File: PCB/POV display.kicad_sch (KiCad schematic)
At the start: 23 parts, among them U1 ESP32-C3FH4, U2 SC7A20, X1 40MHz, 15pF

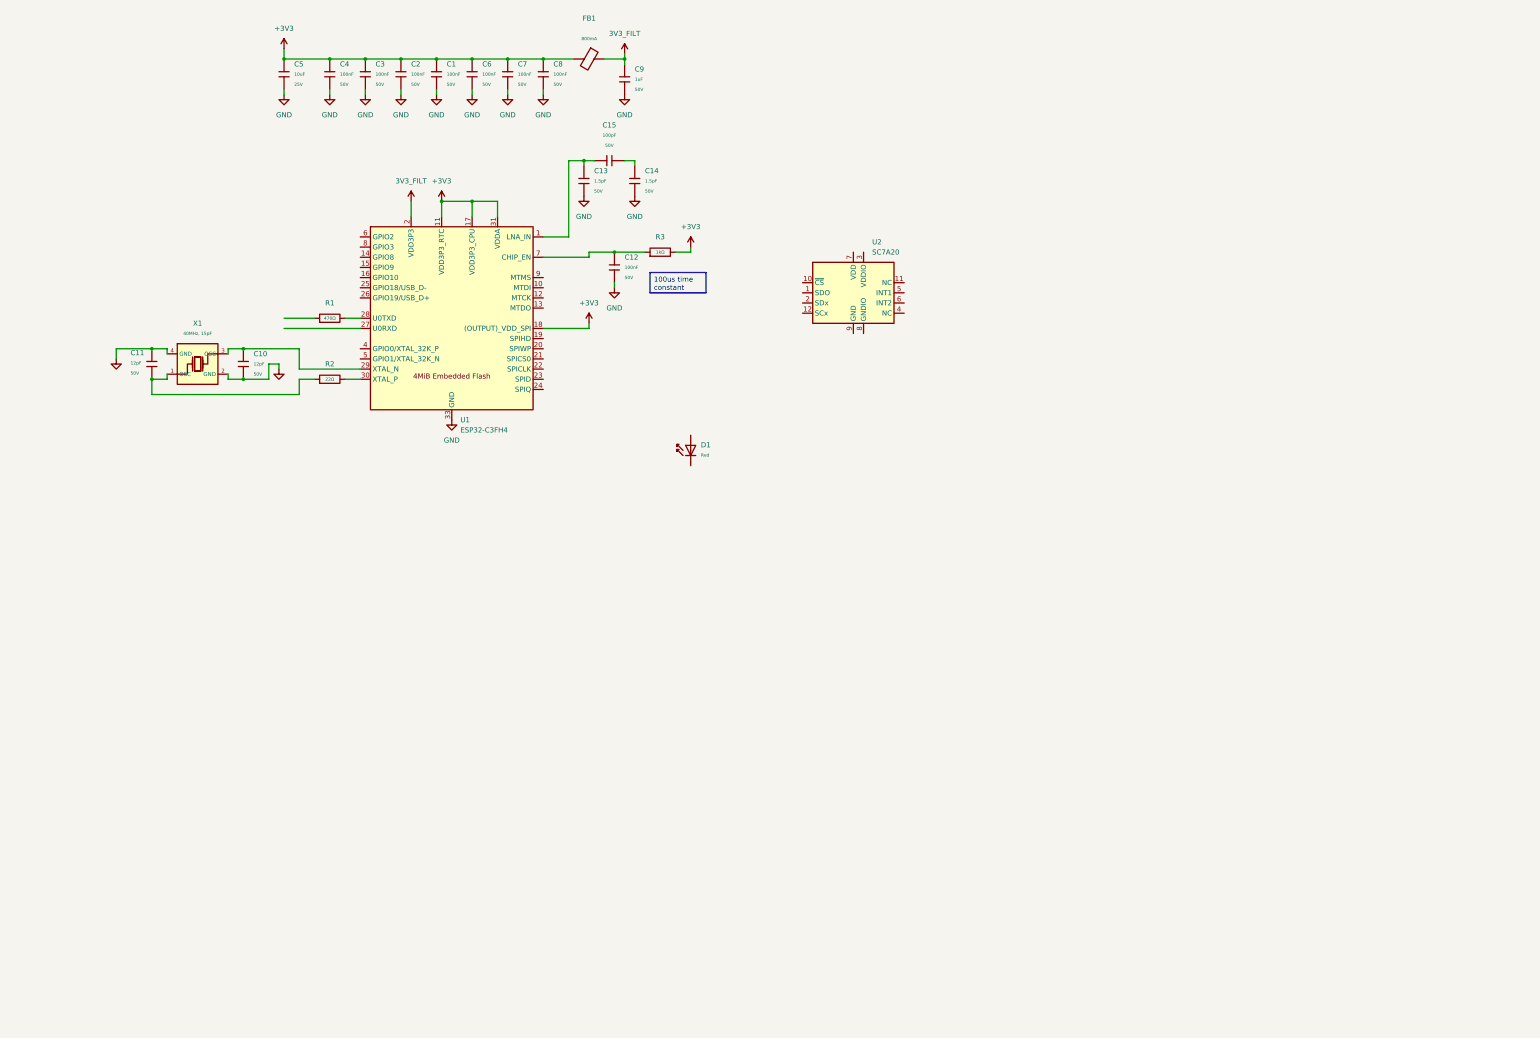
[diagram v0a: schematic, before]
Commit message: added CH570 mcu
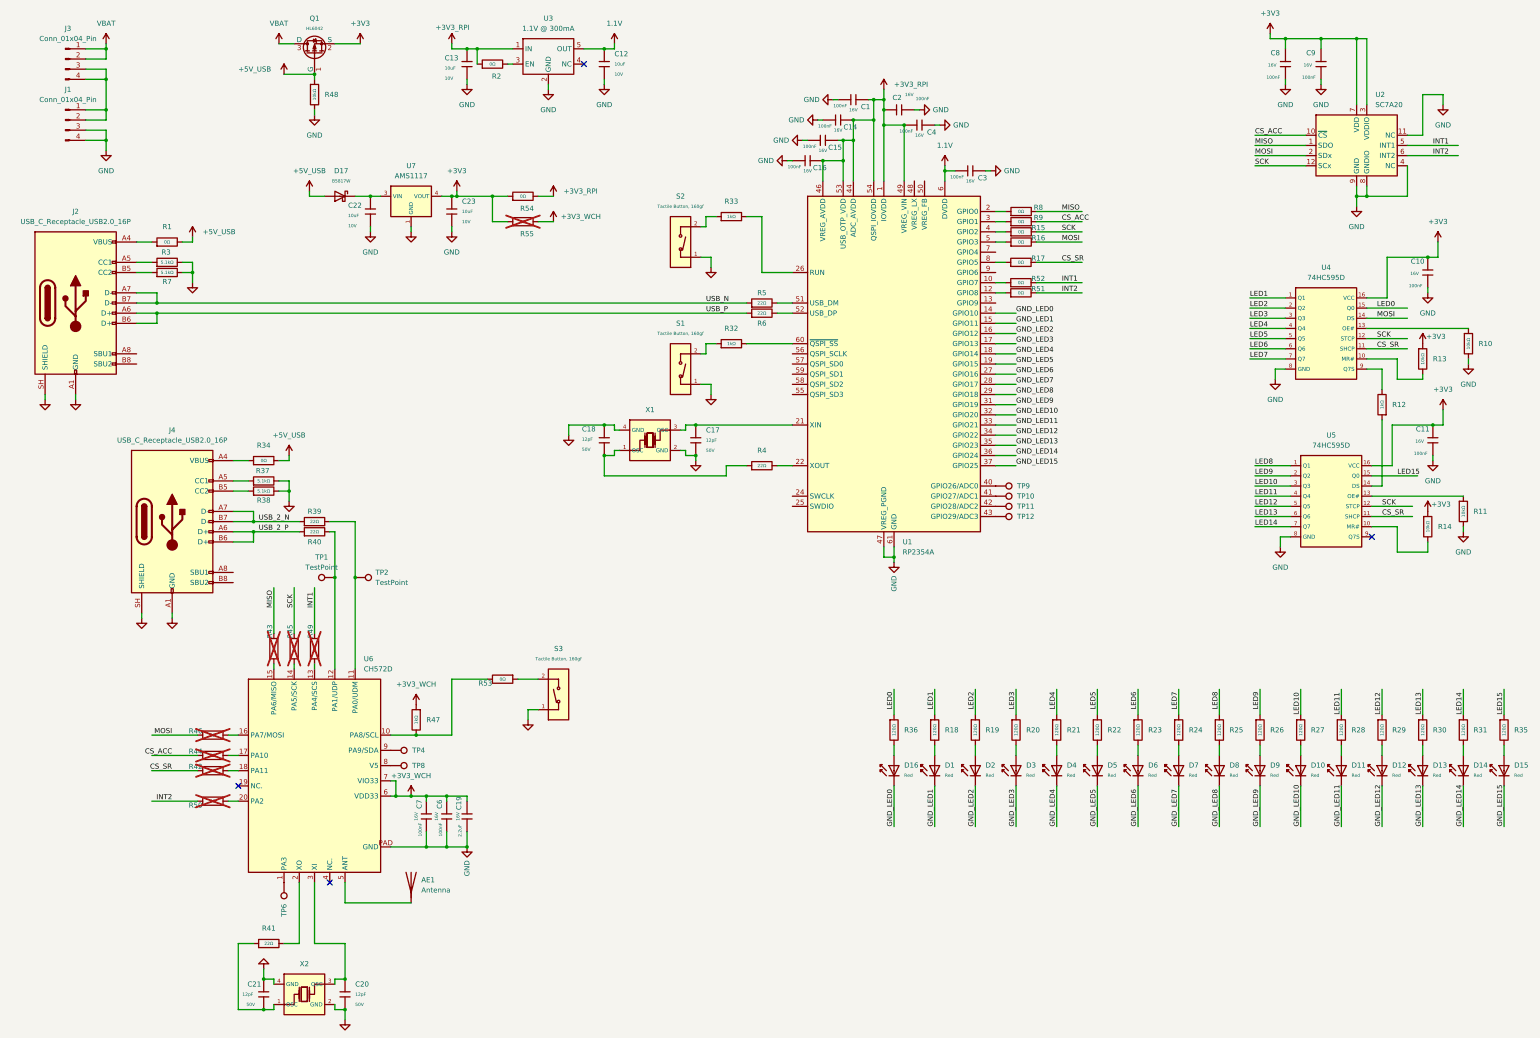
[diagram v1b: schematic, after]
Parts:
- removed C1, C12, C2, C3, C4, C6, C7, C8: 100nF, PCM_JLCPCB:C_0603, symbol PCM_JLCPCB-Capacitors:0603,100nF
- removed C10, C11: 12pF, PCM_JLCPCB:C_0402, symbol PCM_JLCPCB-Capacitors:0402,12pF
- removed C13, C14: 1.5pF, PCM_JLCPCB:C_0402, symbol PCM_JLCPCB-Capacitors:0402,1.5pF
- removed C15: 100pF, PCM_JLCPCB:C_0402, symbol PCM_JLCPCB-Capacitors:0402,100pF
- removed C5: 10uF, PCM_JLCPCB:C_0805, symbol PCM_JLCPCB-Capacitors:0805,10uF
- removed C9: 1uF, PCM_JLCPCB:C_0603, symbol PCM_JLCPCB-Capacitors:0603,1uF
- removed FB1: ~, PCM_JLCPCB:FB_0805, symbol PCM_JLCPCB-Inductors:Ferrite,0805
- removed R1: 470Ω, PCM_JLCPCB:R_0603, symbol PCM_JLCPCB-Resistors:0603,470Ω
- removed R2: 22Ω, PCM_JLCPCB:R_0402, symbol PCM_JLCPCB-Resistors:0402,22Ω
- removed R3: 1kΩ, PCM_JLCPCB:R_0603, symbol PCM_JLCPCB-Resistors:0603,1kΩ
- removed U1: ESP32-C3FH4, PCM_JLCPCB:QFN-32-1EP_5x5mm_P0.5mm_EP3.7x3.7mm_ThermalVias, symbol PCM_JLCPCB-Extended:MCU, ESP32-C3FH4
- removed X1: 40MHz, 15pF, PCM_JLCPCB:OSC-SMD_4P-L3.2-W2.5-BL_SIT8008BI, symbol PCM_JLCPCB-Extended:Crystal, 40MHz, 15pF
- added AE1: Antenna, symbol Device:Antenna
- added C1, C10, C11, C14, C15, C16, C2, C3, C4, C6, C7, C8, C9: 100nF, PCM_JLCPCB:C_0402, symbol PCM_JLCPCB-Capacitors:0402,100nF
- added C12, C13, C22, C23: 10uF, PCM_JLCPCB:C_0603, symbol PCM_JLCPCB-Capacitors:0603,10uF
- added C17, C18, C20, C21: 12pF, PCM_JLCPCB:C_0402, symbol PCM_JLCPCB-Capacitors:0402,12pF
- added C19: 2.2uF, PCM_JLCPCB:C_0603, symbol PCM_JLCPCB-Capacitors:0603,2.2uF
- added D10, D11, D12, D13, D14, D15, D16, D2, D3, D4, D5, D6, D7, D8, D9: Red, PCM_JLCPCB:D_0603, symbol PCM_JLCPCB-Diodes:LED,0603,Red
- added D17: B5817W, PCM_JLCPCB:D_SOD-123, symbol PCM_JLCPCB-Diodes:Schottky,B5817W
- added J1, J3: Conn_01x04_Pin, _MyLib:BC-8200 AAA Battery clip, symbol Connector:Conn_01x04_Pin
- added J2, J4: USB_C_Receptacle_USB2.0_16P, Connector_USB:USB_C_Receptacle_HRO_TYPE-C-31-M-12, symbol Connector:USB_C_Receptacle_USB2.0_16P
- added Q1: HL6042, PCM_JLCPCB:Q_SOT-23, symbol PCM_JLCPCB-Transistors:PMOS,HL6042
- added R1, R15, R16, R17, R2, R34, R42, R43, R44, R45, R46, R49, R50, R51, R52, R53, R54, R55, R8, R9: 0Ω, PCM_JLCPCB:R_0402, symbol PCM_JLCPCB-Resistors:0402,0Ω
- added R10, R11, R13, R14: 10kΩ, PCM_JLCPCB:R_0603, symbol PCM_JLCPCB-Resistors:0603,10kΩ
- added R12: 1kΩ, PCM_JLCPCB:R_0603, symbol PCM_JLCPCB-Resistors:0603,1kΩ
- added R18, R19, R20, R21, R22, R23, R24, R25, R26, R27, R28, R29, R30, R31, R35, R36: 120Ω, PCM_JLCPCB:R_0603, symbol PCM_JLCPCB-Resistors:0603,120Ω
- added R3, R37, R38, R7: 5.1kΩ, PCM_JLCPCB:R_0402, symbol PCM_JLCPCB-Resistors:0402,5.1kΩ
- added R32, R33, R47: 1kΩ, PCM_JLCPCB:R_0402, symbol PCM_JLCPCB-Resistors:0402,1kΩ
- added R39, R4, R40, R41, R5, R6: 22Ω, PCM_JLCPCB:R_0402, symbol PCM_JLCPCB-Resistors:0402,22Ω
- added R48: 10kΩ, PCM_JLCPCB:R_0402, symbol PCM_JLCPCB-Resistors:0402,10kΩ
- added S1, S2, S3: Tactile Button, 160gf, PCM_JLCPCB:SW_TS-1088-AR02016, symbol PCM_JLCPCB-Connectors_Buttons:Tactile Button, 160gf, 12V, 50mA, 4.0mm
- added TP1, TP10, TP11, TP12, TP2, TP4, TP6, TP8, TP9: TestPoint, TestPoint:TestPoint_Pad_D1.0mm, symbol Connector:TestPoint
- added U1: RP2354A, Package_DFN_QFN:QFN-60-1EP_7x7mm_P0.4mm_EP3.4x3.4mm, symbol MCU_RaspberryPi:RP2354A
- added U3: 1.1V @ 300mA, Package_TO_SOT_SMD:SOT-23-5, symbol 0_MyLib:TLV74311PDBVR
- added U4, U5: 74HC595D, PCM_JLCPCB:SOIC-16_L9.9-W3.9-P1.27-LS6.0-BL, symbol PCM_JLCPCB-ICs:Shift Register, 1 In, 8 Out, 74HC595D,118
- added U6: CH572D, Package_DFN_QFN:QFN-20-1EP_3x3mm_P0.4mm_EP1.65x1.65mm, symbol 0_MyLib:CH572D
- added U7: AMS1117, PCM_JLCPCB:SOT-223-3_L6.5-W3.4-P2.30-LS7.0-BR, symbol PCM_JLCPCB-Power:LDO, 3.3V, 1A
- added X1: X322512MSB4SI, PCM_JLCPCB:CRYSTAL-SMD_4P-L3.2-W2.5-BL, symbol PCM_JLCPCB-Crystals:Crystal, 12MHz, 20pF
- added X2: Y201632MFBCX, Crystal:Crystal_SMD_2016-4Pin_2.0x1.6mm, symbol 0_MyLib:Crystal, 32MHz, 12pF
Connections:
- net +3V3: now also U2.3 (VDDIO), U2.7 (VDD), C10.1, C11.1, C23.1, C8.1, C9.1, Q1.2 (S), R13.1, R14.1, R54.1, R55.1, U4.16 (VCC), U5.16 (VCC), U7.2 (VOUT), U7.4 (VOUT)
- net GND: now also U2.11 (NC), U2.4 (NC), U2.8 (GNDIO), U2.9 (GND), C1.2, C10.2, C11.2, C12.2, C13.2, C14.2, C15.2, C16.2, C17.2, C18.2, C19.2, C2.2, C20.2, C21.2, C22.2, C23.2, C3.1, C4.1, C6.2, C7.2, C8.2, C9.2, J1.3 (Pin_3), J1.4 (Pin_4), J2.A1 (GND), J2.A12 (GND), J2.B1 (GND), J2.B12 (GND), J2.SH (SHIELD), J4.A1 (GND), J4.A12 (GND), J4.B1 (GND), J4.B12 (GND), J4.SH (SHIELD), R10.2, R11.2, R3.2, R37.2, R38.2, R48.2, R7.2, S1.1 (A), S2.1 (A), S3.1 (A), U1.47 (VREG_PGND), U1.61 (GND), U3.2 (GND), U4.8 (GND), U5.8 (GND), U6.PAD (GND), U7.1 (GND), X1.2 (GND), X1.4 (GND), X2.2 (GND), X2.4 (GND)
- net MISO: now reaches U2.1 (SDO)
- net MISO: now also R43.2, R8.2
- net CS_ACC: now reaches U2.10 (~{CS})
- net CS_ACC: now also R44.2, R9.2
- net SCK: now reaches U2.12 (SCx)
- net SCK: now also R15.2, R45.2, U4.12 (STCP), U5.12 (STCP)
- net MOSI: now reaches U2.2 (SDx)
- net MOSI: now also R16.2, R46.2, U4.14 (DS)
- net INT1: now reaches U2.5 (INT1)
- net INT1: now also R49.2
- net INT2: now reaches U2.6 (INT2)
- net INT2: now also R50.2
- net GND_LED1: now reaches D1.1
- net GND_LED1: now also U1.15 (GPIO11)
- net at D1.2: now also R18.2
- new net: R39.2, TP2.1, U6.11 (PA0/UDM)
- new net: C22.1, D17.1, U7.3 (VIN)
- new net: D12.2, R29.2
- new net: C21.1, R41.1, X2.1 (OSC)
- new net: D3.2, R20.2
- new net: D4.2, R21.2
- new net: R14.2, U5.10 (MR#)
- new net: D13.2, R30.2
- new net: D15.2, R35.2
- new net: TP8.1, U6.8 (V5)
- new net: R11.1, U5.13 (OE#)
- new net: R53.1, S3.2 (B)
- new net: R47.2, R53.2, U6.10 (PA8/SCL)
- new net: D10.2, R27.2
- new net: R17.1, U1.8 (GPIO5)
- new net: R32.1, S1.2 (B)
- new net: R32.2, U1.60 (~{QSPI_SS})
- new net: C18.1, R4.1, X1.1 (OSC)
- new net: R4.2, U1.22 (XOUT)
- new net: D6.2, R23.2
- new net: J1.1 (Pin_1), J1.2 (Pin_2), J3.3 (Pin_3), J3.4 (Pin_4)
- new net: D8.2, R25.2
- new net: AE1.1 (A), U6.5 (ANT)
- new net: R41.2, U6.2 (XO)
- new net: D16.2, R36.2
- new net: R40.2, TP1.1, U6.12 (PA1/UDP)
- new net: D9.2, R26.2
- new net: TP6.1, U6.1 (PA3)
- new net: J4.A4 (VBUS), J4.A9 (VBUS), J4.B4 (VBUS), J4.B9 (VBUS), R34.1
- new net: R50.1, U6.20 (PA2)
- new net: R13.2, U4.10 (MR#)
- new net: D2.2, R19.2
- new net: D14.2, R31.2
- new net: D5.2, R22.2
- new net: R8.1, U1.2 (GPIO0)
- new net: TP11.1, U1.42 (GPIO28/ADC2)
- new net: TP4.1, U6.9 (PA9/SDA)
- new net: J4.A5 (CC1), R37.1
- new net: J4.B5 (CC2), R38.1
- new net: R46.1, U6.16 (PA7/MOSI)
- new net: R12.1, U5.14 (DS)
- new net: R52.1, U1.10 (GPIO7)
- new net: R51.1, U1.12 (GPIO8)
- new net: C17.1, U1.21 (XIN), X1.3 (OSC)
- new net: R33.2, U1.26 (RUN)
- new net: R9.1, U1.3 (GPIO1)
- new net: R15.1, U1.4 (GPIO2)
- new net: TP9.1, U1.40 (GPIO26/ADC0)
- new net: TP10.1, U1.41 (GPIO27/ADC1)
- new net: TP12.1, U1.43 (GPIO29/ADC3)
- new net: R16.1, U1.5 (GPIO3)
- new net: R5.2, U1.51 (USB_DM)
- new net: R6.2, U1.52 (USB_DP)
- new net: J2.A4 (VBUS), J2.A9 (VBUS), J2.B4 (VBUS), J2.B9 (VBUS), R1.1
- new net: R2.2, U3.3 (EN)
- new net: C20.1, U6.3 (XI), X2.3 (OSC)
- new net: J2.B5 (CC2), R7.1
- new net: R42.1, U6.18 (PA11)
- new net: R43.1, U6.15 (PA6/MISO)
- new net: D11.2, R28.2
- new net: R33.1, S2.2 (B)
- new net: R12.2, U4.9 (Q7S)
- new net: R10.1, U4.13 (OE#)
- new net: R44.1, U6.17 (PA10)
- new net: D7.2, R24.2
- new net: J2.A5 (CC1), R3.1
- new net: R45.1, U6.14 (PA5/SCK)
- new net: R49.1, U6.13 (PA4/SCS)
- new net +3V3_RPI: C1.1, C13.1, C14.1, C15.1, C16.1, C2.1, C4.2, R2.1, R54.2, U1.1 (IOVDD), U1.11 (IOVDD), U1.20 (IOVDD), U1.30 (IOVDD), U1.38 (IOVDD), U1.44 (ADC_AVDD), U1.45 (IOVDD), U1.46 (VREG_AVDD), U1.49 (VREG_VIN), U1.53 (USB_OTP_VDD), U1.54 (QSPI_IOVDD), U3.1 (IN)
- new net +3V3_WCH: C19.1, C6.1, C7.1, R47.1, R55.2, U6.6 (VDD33), U6.7 (VIO33)
- new net +5V_USB: D17.2, Q1.1 (G), R1.2, R34.2, R48.1
- new net 1.1V: C12.1, C3.2, U1.23 (DVDD), U1.39 (DVDD), U1.6 (DVDD), U3.5 (OUT)
- new net CS_SR: R17.2, R42.2, U4.11 (SHCP), U5.11 (SHCP)
- new net GND_LED0: D16.1, U1.14 (GPIO10)
- new net GND_LED10: D10.1, U1.32 (GPIO20)
- new net GND_LED11: D11.1, U1.33 (GPIO21)
- new net GND_LED12: D12.1, U1.34 (GPIO22)
- new net GND_LED13: D13.1, U1.35 (GPIO23)
- new net GND_LED14: D14.1, U1.36 (GPIO24)
- new net GND_LED15: D15.1, U1.37 (GPIO25)
- new net GND_LED2: D2.1, U1.16 (GPIO12)
- new net GND_LED3: D3.1, U1.17 (GPIO13)
- new net GND_LED4: D4.1, U1.18 (GPIO14)
- new net GND_LED5: D5.1, U1.19 (GPIO15)
- new net GND_LED6: D6.1, U1.27 (GPIO16)
- new net GND_LED7: D7.1, U1.28 (GPIO17)
- new net GND_LED8: D8.1, U1.29 (GPIO18)
- new net GND_LED9: D9.1, U1.31 (GPIO19)
- new net LED0: R36.1, U4.15 (Q0)
- new net LED1: R18.1, U4.1 (Q1)
- new net LED10: R27.1, U5.3 (Q3)
- new net LED11: R28.1, U5.4 (Q4)
- new net LED12: R29.1, U5.5 (Q5)
- new net LED13: R30.1, U5.6 (Q6)
- new net LED14: R31.1, U5.7 (Q7)
- new net LED15: R35.1, U5.15 (Q0)
- new net LED2: R19.1, U4.2 (Q2)
- new net LED3: R20.1, U4.3 (Q3)
- new net LED4: R21.1, U4.4 (Q4)
- new net LED5: R22.1, U4.5 (Q5)
- new net LED6: R23.1, U4.6 (Q6)
- new net LED7: R24.1, U4.7 (Q7)
- new net LED8: R25.1, U5.1 (Q1)
- new net LED9: R26.1, U5.2 (Q2)
- new net USB_2_N: J4.A7 (D-), J4.B7 (D-), R39.1
- new net USB_2_P: J4.A6 (D+), J4.B6 (D+), R40.1
- new net USB_N: J2.A7 (D-), J2.B7 (D-), R5.1
- new net USB_P: J2.A6 (D+), J2.B6 (D+), R6.1
- new net VBAT: J3.1 (Pin_1), J3.2 (Pin_2), Q1.3 (D)
- no-connect marks 0 -> 4
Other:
- moved on the sheet: D1, U2

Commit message: firmware initial complete
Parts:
- removed AE1: Antenna, symbol Device:Antenna
- removed TP1, TP2: TestPoint, TestPoint:TestPoint_Pad_D1.0mm, symbol Connector:TestPoint
- added AE1: Antenna_Chip, Capacitor_SMD:C_1206_3216Metric, symbol Device:Antenna_Chip
- added C24, C25, C26, C5: 100nF, PCM_JLCPCB:C_0402, symbol PCM_JLCPCB-Capacitors:0402,100nF
- added TP13, TP14: TestPoint, TestPoint:TestPoint_Pad_D1.0mm, symbol Connector:TestPoint
- U2: LCSC (none) -> C19274408
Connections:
- net +3V3_RPI: now also C25.1, C26.1
- net 1.1V: now also C24.2, C5.2
- net GND: now also U6.21 (GND), C24.1, C25.2, C26.2, C5.1; no longer U6.PAD (GND)
- net GND_LED0: now also U1.29 (GPIO18); no longer U1.14 (GPIO10)
- net GND_LED1: now also U1.28 (GPIO17); no longer U1.15 (GPIO11)
- net GND_LED10: now also U1.12 (GPIO8); no longer U1.32 (GPIO20)
- net GND_LED11: now also U1.10 (GPIO7); no longer U1.33 (GPIO21)
- net GND_LED12: now also U1.9 (GPIO6); no longer U1.34 (GPIO22)
- net GND_LED13: now also U1.8 (GPIO5); no longer U1.35 (GPIO23)
- net GND_LED14: now also U1.7 (GPIO4); no longer U1.36 (GPIO24)
- net GND_LED15: now also U1.5 (GPIO3); no longer U1.37 (GPIO25)
- net GND_LED2: now also U1.27 (GPIO16); no longer U1.16 (GPIO12)
- net GND_LED3: now also U1.19 (GPIO15); no longer U1.17 (GPIO13)
- net GND_LED5: now also U1.17 (GPIO13); no longer U1.19 (GPIO15)
- net GND_LED6: now also U1.16 (GPIO12); no longer U1.27 (GPIO16)
- net GND_LED7: now also U1.15 (GPIO11); no longer U1.28 (GPIO17)
- net GND_LED8: now also U1.14 (GPIO10); no longer U1.29 (GPIO18)
- net GND_LED9: now also U1.13 (GPIO9); no longer U1.31 (GPIO19)
- net INT1: now also R52.2
- net INT2: now also R51.2
- net at R17.1: now also U1.37 (GPIO25); no longer U1.8 (GPIO5)
- net at U6.5 (ANT): now also AE1.2 (PCB_Trace)
- net at R8.1: now also U1.32 (GPIO20); no longer U1.2 (GPIO0)
- net at R52.1: now also U1.35 (GPIO23); no longer U1.10 (GPIO7)
- net at R51.1: now also U1.33 (GPIO21); no longer U1.12 (GPIO8)
- net at U1.24 (SWCLK): now also TP13.1
- net at U1.25 (SWDIO): now also TP14.1
- net at U1.3 (GPIO1): no longer R9.1
- net at R15.1: now also U1.34 (GPIO22); no longer U1.4 (GPIO2)
- net at R16.1: now also U1.31 (GPIO19); no longer U1.5 (GPIO3)
- new net: R9.1, U1.36 (GPIO24)
- no-connect marks 4 -> 5
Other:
- moved on the sheet: R15, R16, R17, R51, R52, R8, R9
